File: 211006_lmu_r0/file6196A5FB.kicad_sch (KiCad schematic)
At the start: 8 parts, among them U4 LTC3300ILXE-2#PBF

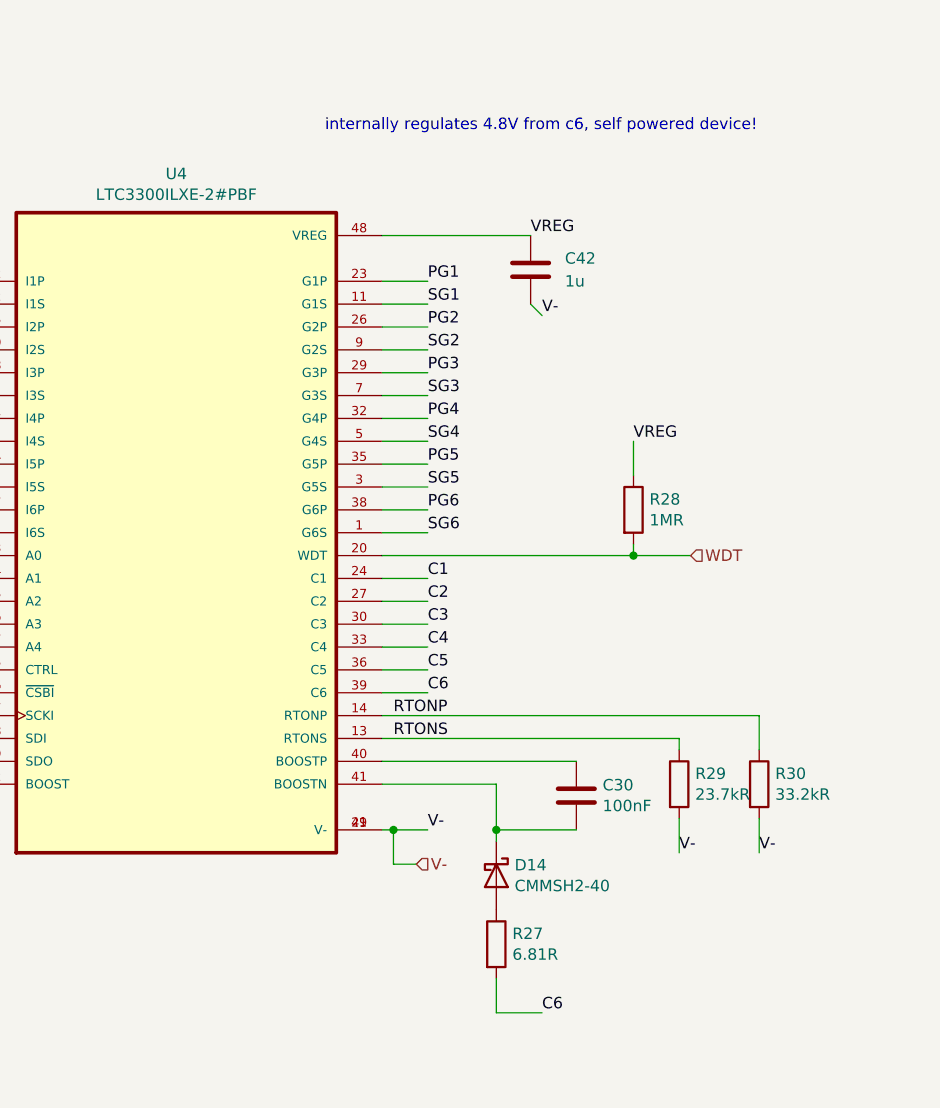
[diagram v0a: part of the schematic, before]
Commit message: routed ltc3811 accessories
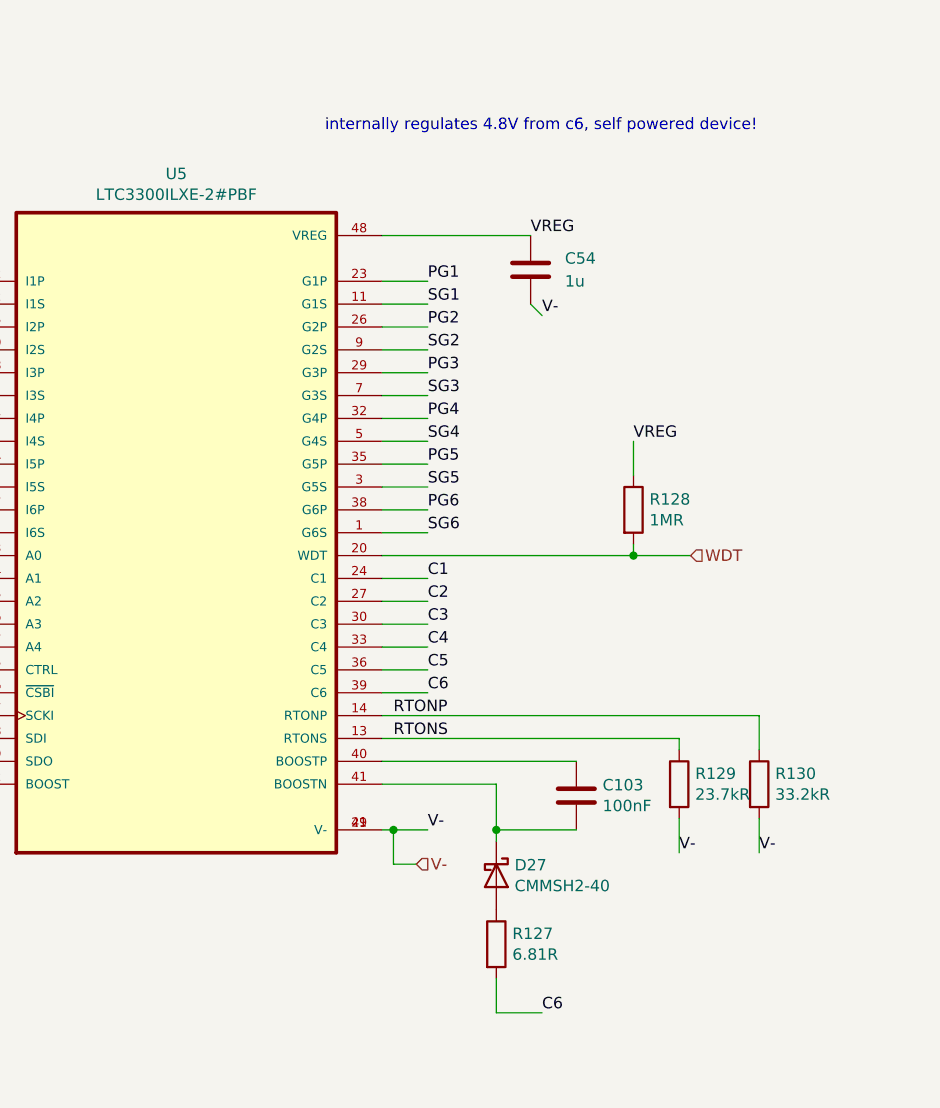
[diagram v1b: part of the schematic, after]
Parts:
- renumbered C30 to C103, C42 to C54, D14 to D27, R27 to R127, R28 to R128, R29 to R129, R30 to R130, U4 to U5
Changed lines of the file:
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@@
   (symbol (lib_id "Device:R") (at 260.35 114.3 0)
     (in_bom yes) (on_board yes)
-    (property "Reference" "R29" (id 0) (at 262.128 113.1316 0)
+    (property "Reference" "R129" (id 0) (at 262.128 113.1316 0)
       (effects (font (size 1.27 1.27)) (justify left))
     )
@@
   (symbol (lib_id "Device:D_Schottky") (at 240.03 124.46 270)
     (in_bom yes) (on_board yes)
-    (property "Reference" "D14" (id 0) (at 242.062 123.2916 90)
+    (property "Reference" "D27" (id 0) (at 242.062 123.2916 90)
       (effects (font (size 1.27 1.27)) (justify left))
     )
@@
   (symbol (lib_id "Device:R") (at 240.03 132.08 0)
     (in_bom yes) (on_board yes)
-    (property "Reference" "R27" (id 0) (at 241.808 130.9116 0)
+    (property "Reference" "R127" (id 0) (at 241.808 130.9116 0)
       (effects (font (size 1.27 1.27)) (justify left))
     )
@@
   (symbol (lib_id "Device:C") (at 248.92 115.57 0)
     (in_bom yes) (on_board yes)
-    (property "Reference" "C30" (id 0) (at 251.841 114.4016 0)
+    (property "Reference" "C103" (id 0) (at 251.841 114.4016 0)
       (effects (font (size 1.27 1.27)) (justify left))
     )
@@
   (symbol (lib_id "LTC3300ILXE-2_PBF:LTC3300ILXE-2#PBF") (at 204.47 86.36 0)
     (in_bom yes) (on_board yes)
-    (property "Reference" "U4" (id 0) (at 204.47 46.482 0))
+    (property "Reference" "U5" (id 0) (at 204.47 46.482 0))
     (property "Value" "LTC3300ILXE-2#PBF" (id 1) (at 204.47 48.7934 0))
     (property "Footprint" "LTC3300ILXE-2_PBF:QFP50P900X900X160-49N" (id 2) (at 204.47 86.36 0)
@@
   (symbol (lib_id "Device:R") (at 269.24 114.3 0)
     (in_bom yes) (on_board yes)
-    (property "Reference" "R30" (id 0) (at 271.018 113.1316 0)
+    (property "Reference" "R130" (id 0) (at 271.018 113.1316 0)
       (effects (font (size 1.27 1.27)) (justify left))
     )
@@
   (symbol (lib_id "Device:R") (at 255.27 83.82 0)
     (in_bom yes) (on_board yes)
-    (property "Reference" "R28" (id 0) (at 257.048 82.6516 0)
+    (property "Reference" "R128" (id 0) (at 257.048 82.6516 0)
       (effects (font (size 1.27 1.27)) (justify left))
     )
@@
   (symbol (lib_id "Device:C") (at 243.84 57.15 0)
     (in_bom yes) (on_board yes) (fields_autoplaced)
-    (property "Reference" "C42" (id 0) (at 247.65 55.8799 0)
-      (effects (font (size 1.27 1.27)) (justify left))
-    )
+    (property "Reference" "C54" (id 0) (at 247.65 55.8799 0)
+      (effects (font (size 1.27 1.27)) (justify left))
+    )

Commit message: going to bulk edit fields
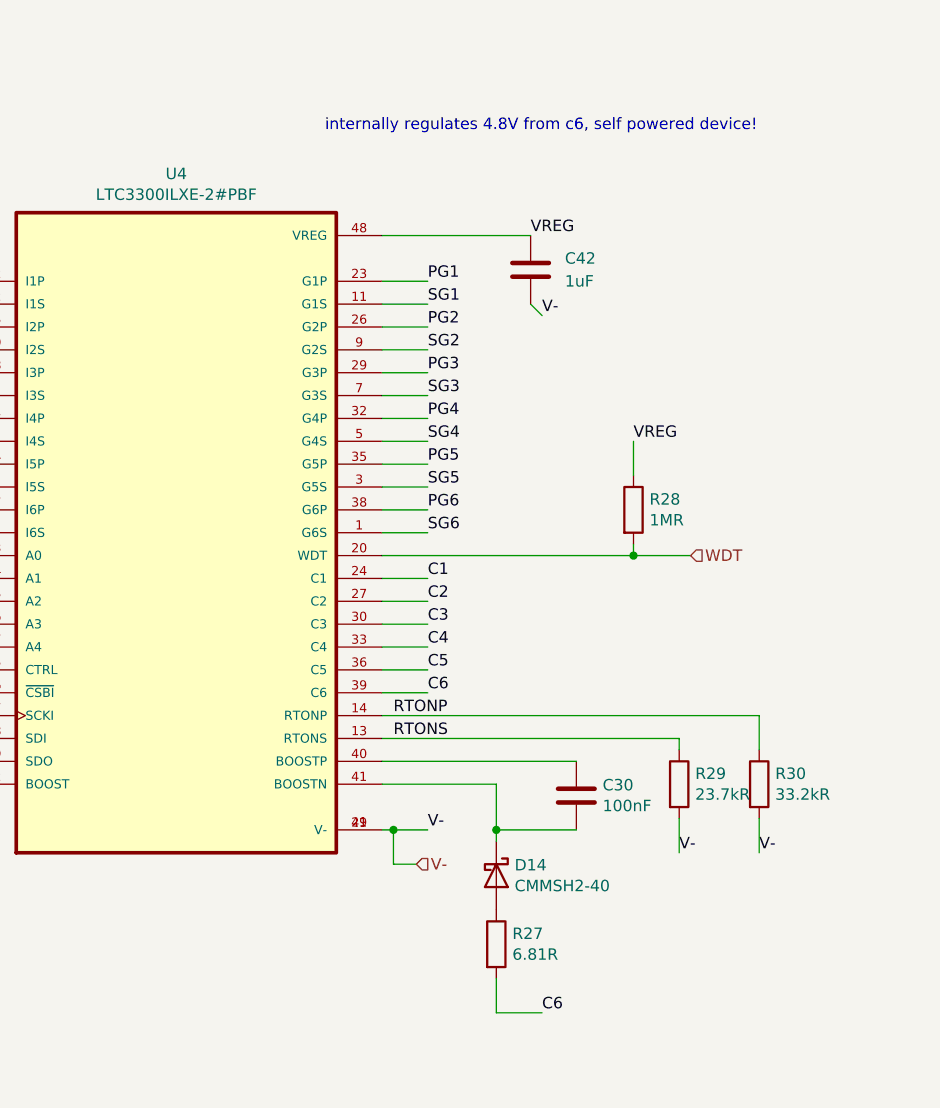
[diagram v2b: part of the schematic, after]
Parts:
- C42: renamed from C54; value 1u -> 1uF
- R27: renamed from R127; footprint Resistor_SMD:R_0603_1608Metric_Pad0.98x0.95mm_HandSolder -> Resistor_SMD:R_1206_3216Metric_Pad1.30x1.75mm_HandSolder
- U4: renamed from U5; AVAILABILITY Unavailable -> (none)
- renumbered C103 to C30, D27 to D14, R128 to R28, R129 to R29, R130 to R30
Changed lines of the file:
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@@
   (symbol (lib_id "Device:R") (at 260.35 114.3 0)
     (in_bom yes) (on_board yes)
-    (property "Reference" "R129" (id 0) (at 262.128 113.1316 0)
+    (property "Reference" "R29" (id 0) (at 262.128 113.1316 0)
       (effects (font (size 1.27 1.27)) (justify left))
     )
@@
   (symbol (lib_id "Device:D_Schottky") (at 240.03 124.46 270)
     (in_bom yes) (on_board yes)
-    (property "Reference" "D27" (id 0) (at 242.062 123.2916 90)
+    (property "Reference" "D14" (id 0) (at 242.062 123.2916 90)
       (effects (font (size 1.27 1.27)) (justify left))
     )
@@
   (symbol (lib_id "Device:R") (at 240.03 132.08 0)
     (in_bom yes) (on_board yes)
-    (property "Reference" "R127" (id 0) (at 241.808 130.9116 0)
+    (property "Reference" "R27" (id 0) (at 241.808 130.9116 0)
       (effects (font (size 1.27 1.27)) (justify left))
     )
@@
       (effects (font (size 1.27 1.27)) (justify left))
     )
-    (property "Footprint" "Resistor_SMD:R_0603_1608Metric_Pad0.98x0.95mm_HandSolder" (id 2) (at 238.252 132.08 90)
+    (property "Footprint" "Resistor_SMD:R_1206_3216Metric_Pad1.30x1.75mm_HandSolder" (id 2) (at 238.252 132.08 90)
       (effects (font (size 1.27 1.27)) hide)
     )
@@
   (symbol (lib_id "Device:C") (at 248.92 115.57 0)
     (in_bom yes) (on_board yes)
-    (property "Reference" "C103" (id 0) (at 251.841 114.4016 0)
+    (property "Reference" "C30" (id 0) (at 251.841 114.4016 0)
       (effects (font (size 1.27 1.27)) (justify left))
     )
@@
   (symbol (lib_id "LTC3300ILXE-2_PBF:LTC3300ILXE-2#PBF") (at 204.47 86.36 0)
     (in_bom yes) (on_board yes)
-    (property "Reference" "U5" (id 0) (at 204.47 46.482 0))
+    (property "Reference" "U4" (id 0) (at 204.47 46.482 0))
     (property "Value" "LTC3300ILXE-2#PBF" (id 1) (at 204.47 48.7934 0))
     (property "Footprint" "LTC3300ILXE-2_PBF:QFP50P900X900X160-49N" (id 2) (at 204.47 86.36 0)
@@
       (effects (font (size 1.27 1.27)) (justify left bottom) hide)
     )
-    (property "AVAILABILITY" "Unavailable" (id 11) (at 204.47 86.36 0)
+    (property "AVAILABILITY" "" (id 11) (at 204.47 86.36 0)
       (effects (font (size 1.27 1.27)) (justify left bottom) hide)
     )
@@
   (symbol (lib_id "Device:R") (at 269.24 114.3 0)
     (in_bom yes) (on_board yes)
-    (property "Reference" "R130" (id 0) (at 271.018 113.1316 0)
+    (property "Reference" "R30" (id 0) (at 271.018 113.1316 0)
       (effects (font (size 1.27 1.27)) (justify left))
     )
@@
   (symbol (lib_id "Device:R") (at 255.27 83.82 0)
     (in_bom yes) (on_board yes)
-    (property "Reference" "R128" (id 0) (at 257.048 82.6516 0)
+    (property "Reference" "R28" (id 0) (at 257.048 82.6516 0)
       (effects (font (size 1.27 1.27)) (justify left))
     )
@@
   (symbol (lib_id "Device:C") (at 243.84 57.15 0)
     (in_bom yes) (on_board yes) (fields_autoplaced)
-    (property "Reference" "C54" (id 0) (at 247.65 55.8799 0)
-      (effects (font (size 1.27 1.27)) (justify left))
-    )
-    (property "Value" "1u" (id 1) (at 247.65 58.4199 0)
-      (effects (font (size 1.27 1.27)) (justify left))
-    )
+    (property "Reference" "C42" (id 0) (at 247.65 55.8799 0)
+      (effects (font (size 1.27 1.27)) (justify left))
+    )
+    (property "Value" "1uF" (id 1) (at 247.65 58.4199 0)
+      (effects (font (size 1.27 1.27)) (justify left))
+    )

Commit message: started to export and fix things
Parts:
- C54: renamed from C42; Manufacturer (none) -> -; Part Number (none) -> -
- U5: renamed from U4; MANUFACTURER Linear Technology -> (none); MP LTC3300ILXE-2#PBF -> (none); PACKAGE LQFP-48 Linear Technology -> (none); PARTREV A -> (none); PRICE 10.07 USD -> (none); SNAPEDA_PACKAGE_ID 29275 -> (none); STANDARD IPC-7351B -> (none)
- renumbered C30 to C103, D14 to D27, R27 to R127, R28 to R128, R29 to R129, R30 to R130
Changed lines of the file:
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@@
   (symbol (lib_id "Device:R") (at 260.35 114.3 0)
     (in_bom yes) (on_board yes)
-    (property "Reference" "R29" (id 0) (at 262.128 113.1316 0)
+    (property "Reference" "R129" (id 0) (at 262.128 113.1316 0)
       (effects (font (size 1.27 1.27)) (justify left))
     )
@@
   (symbol (lib_id "Device:D_Schottky") (at 240.03 124.46 270)
     (in_bom yes) (on_board yes)
-    (property "Reference" "D14" (id 0) (at 242.062 123.2916 90)
+    (property "Reference" "D27" (id 0) (at 242.062 123.2916 90)
       (effects (font (size 1.27 1.27)) (justify left))
     )
@@
   (symbol (lib_id "Device:R") (at 240.03 132.08 0)
     (in_bom yes) (on_board yes)
-    (property "Reference" "R27" (id 0) (at 241.808 130.9116 0)
+    (property "Reference" "R127" (id 0) (at 241.808 130.9116 0)
       (effects (font (size 1.27 1.27)) (justify left))
     )
@@
   (symbol (lib_id "Device:C") (at 248.92 115.57 0)
     (in_bom yes) (on_board yes)
-    (property "Reference" "C30" (id 0) (at 251.841 114.4016 0)
+    (property "Reference" "C103" (id 0) (at 251.841 114.4016 0)
       (effects (font (size 1.27 1.27)) (justify left))
     )
@@
   (symbol (lib_id "LTC3300ILXE-2_PBF:LTC3300ILXE-2#PBF") (at 204.47 86.36 0)
     (in_bom yes) (on_board yes)
-    (property "Reference" "U4" (id 0) (at 204.47 46.482 0))
+    (property "Reference" "U5" (id 0) (at 204.47 46.482 0))
     (property "Value" "LTC3300ILXE-2#PBF" (id 1) (at 204.47 48.7934 0))
     (property "Footprint" "LTC3300ILXE-2_PBF:QFP50P900X900X160-49N" (id 2) (at 204.47 86.36 0)
@@
     )
     (property "Datasheet" "" (id 3) (at 204.47 86.36 0)
-      (effects (font (size 1.27 1.27)) (justify left bottom) hide)
-    )
-    (property "PACKAGE" "LQFP-48 Linear Technology" (id 4) (at 204.47 86.36 0)
-      (effects (font (size 1.27 1.27)) (justify left bottom) hide)
-    )
-    (property "SNAPEDA_PACKAGE_ID" "29275" (id 5) (at 204.47 86.36 0)
-      (effects (font (size 1.27 1.27)) (justify left bottom) hide)
-    )
-    (property "STANDARD" "IPC-7351B" (id 6) (at 204.47 86.36 0)
-      (effects (font (size 1.27 1.27)) (justify left bottom) hide)
-    )
-    (property "PRICE" "10.07 USD" (id 7) (at 204.47 86.36 0)
-      (effects (font (size 1.27 1.27)) (justify left bottom) hide)
-    )
-    (property "MP" "LTC3300ILXE-2#PBF" (id 8) (at 204.47 86.36 0)
-      (effects (font (size 1.27 1.27)) (justify left bottom) hide)
-    )
-    (property "PARTREV" "A" (id 9) (at 204.47 86.36 0)
-      (effects (font (size 1.27 1.27)) (justify left bottom) hide)
-    )
-    (property "MANUFACTURER" "Linear Technology" (id 10) (at 204.47 86.36 0)
-      (effects (font (size 1.27 1.27)) (justify left bottom) hide)
-    )
-    (property "AVAILABILITY" "" (id 11) (at 204.47 86.36 0)
       (effects (font (size 1.27 1.27)) (justify left bottom) hide)
     )
@@
   (symbol (lib_id "Device:R") (at 269.24 114.3 0)
     (in_bom yes) (on_board yes)
-    (property "Reference" "R30" (id 0) (at 271.018 113.1316 0)
+    (property "Reference" "R130" (id 0) (at 271.018 113.1316 0)
       (effects (font (size 1.27 1.27)) (justify left))
     )
@@
   (symbol (lib_id "Device:R") (at 255.27 83.82 0)
     (in_bom yes) (on_board yes)
-    (property "Reference" "R28" (id 0) (at 257.048 82.6516 0)
+    (property "Reference" "R128" (id 0) (at 257.048 82.6516 0)
       (effects (font (size 1.27 1.27)) (justify left))
     )
@@
   (symbol (lib_id "Device:C") (at 243.84 57.15 0)
     (in_bom yes) (on_board yes) (fields_autoplaced)
-    (property "Reference" "C42" (id 0) (at 247.65 55.8799 0)
+    (property "Reference" "C54" (id 0) (at 247.65 55.8799 0)
       (effects (font (size 1.27 1.27)) (justify left))
     )
@@
       (effects (font (size 1.27 1.27)) hide)
     )
+    (property "Manufacturer" "-" (id 4) (at 243.84 57.15 0)
+      (effects (font (size 1.27 1.27)) hide)
+    )
+    (property "Part Number" "-" (id 5) (at 243.84 57.15 0)
+      (effects (font (size 1.27 1.27)) hide)
+    )
